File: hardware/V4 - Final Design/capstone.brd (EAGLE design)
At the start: 68.6 x 51.3 mm, 32 parts, among them J1 61300311121, J2 61300311121, J3 61300311121, U1 BMP388, U2 LSM9DS1TR, U3 RFM95W-915S2

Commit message: Schematic Cleanup
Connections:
- net +3V3: now also C3.1; no longer C3.2
- net GND: now also C3.2; no longer C3.1
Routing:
- net +3V3: track 117.5 -> 98.0 mm, vias 3 -> 2
- net GND: track 169.5 -> 154.7 mm
- net N$4: track 6.48 -> 4.67 mm

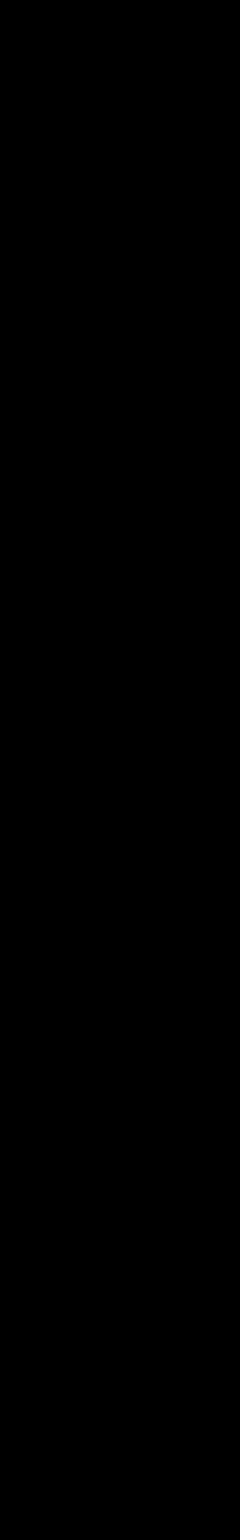
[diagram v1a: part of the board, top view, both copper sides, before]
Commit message: add test points to final design
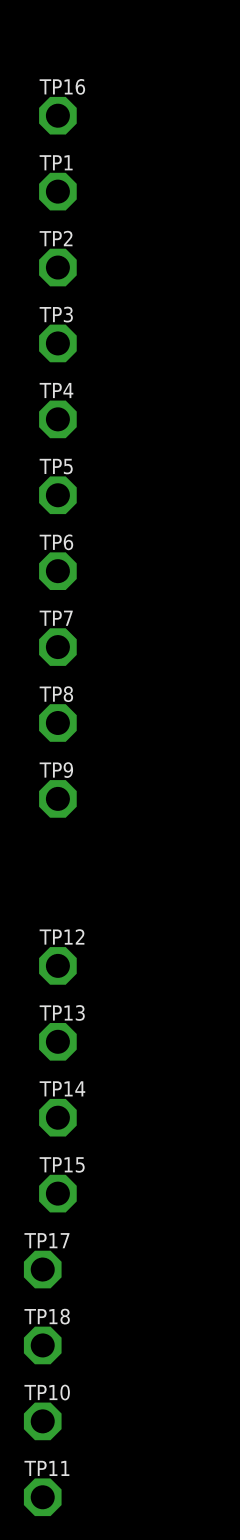
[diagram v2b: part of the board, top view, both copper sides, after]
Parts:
- added TP1, TP10, TP11, TP12, TP13, TP14, TP15, TP16, TP17, TP18, TP2, TP3, TP4, TP5, TP6, TP7, TP8, TP9: PTR1PAD1-20, testpad:P1-20
- R1, R11, R12, R2: value 100 Ohm -> 470 Ohm
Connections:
- net +3V3: now also TP10.TP, TP17.TP, TP4.TP, TP8.TP, TP9.TP
- net GND: now also TP1.TP
- net MISO: now also TP12.TP
- net MOSI: now also TP18.TP
- net RADIO_INT: now also TP15.TP, U$1.15/A1
- net RADIO_RST: now also TP14.TP
- net SCK: now also TP13.TP
- net SCL: now also TP2.TP
- net SDA: now also TP3.TP
- net SERVO1: now also TP5.TP
- net SERVO2: now also TP6.TP
- net SERVO3: now also TP7.TP
- net VBACKUP: now also TP11.TP
- net VIN: now also TP16.TP

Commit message: finalized board design for final design
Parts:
- added H1, H2, H3, H4: MOUNT-HOLE2.8, holes:2,8
- C1, C4: value 10 uF -> 10 u
- C2: value 100 nF -> 100 n
- C3: value 0.1 uF -> 0.1u
- TP1, TP10, TP11, TP12, TP13, TP14, TP15, TP16, TP17, TP18, TP2, TP3, TP4, TP5, TP6, TP7, TP8, TP9: value PTR1PAD1-20 -> PTR1B1,27; device testpad:P1-20 -> testpad:B1,27
- moved TP10 368.1 mm to (63.5, 29.2)
- moved TP17 355.9 mm to (6.35, 39.4)
- moved TP11 354.5 mm to (58.4, 10.2)
- moved TP18 351.5 mm to (23.1, 26.7)
- moved TP13 331.4 mm to (23.4, 31.9)
- moved TP15 328.2 mm to (8.89, 17.8)
- moved TP9 326.6 mm to (39.8, 44.5)
- moved TP14 322.5 mm to (14.0, 17.8)
- moved TP8 318.2 mm to (14.6, 46.5)
- moved TP12 314.7 mm to (23.1, 21.3)
- moved TP3 284.2 mm to (26.7, 41.9)
- moved TP2 277.3 mm to (22.9, 41.9)
- moved TP7 276.7 mm to (19.7, 10.2)
- moved TP6 269.9 mm to (15.9, 10.2)
- moved TP4 264.8 mm to (22.9, 16.5)
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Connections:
- net +3V3: now also TP11.TP; no longer TP10.TP
- net GND: now also TP16.TP; no longer TP1.TP
- net VBACKUP: now also TP10.TP; no longer TP11.TP
- net VIN: now also TP1.TP; no longer TP16.TP
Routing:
- net GPS_TX: track 103.3 -> 21.9 mm
- net GPS_RX: track 101.1 -> 20.0 mm, vias 2 -> 1
- net GND: track 154.7 -> 82.6 mm, vias 11 -> 7
- net RADIO_LED: track 0.00 -> 50.0 mm, vias 0 -> 3
- net ERR_LED: track 0.00 -> 49.8 mm, vias 0 -> 3
- net STATUS_LED: track 0.00 -> 44.5 mm, vias 0 -> 3
- net RADIO_INT: track 0.00 -> 35.6 mm, vias 0 -> 1
- net VIN: track 23.9 -> 56.6 mm
- net RADIO_RST: track 0.00 -> 29.5 mm, vias 0 -> 1
- net VBACKUP: track 0.00 -> 26.9 mm, vias 0 -> 3
- net SERVO1: track 0.00 -> 22.4 mm, vias 0 -> 1
- net +3V3: track 98.0 -> 115.7 mm, vias 2 -> 10
- net SCK: track 35.3 -> 17.7 mm, vias 2 -> 1
- net MISO: track 23.0 -> 39.8 mm, vias 0 -> 2
- net SERVO2: track 0.00 -> 15.9 mm, vias 0 -> 1
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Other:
- board text added: "0.1u"
- board text added: "100n"
- board text added: "10n"
- board text added: "10u"
- board text added: "4.7k"
- board text added: "470"
- board text added: "ANT"
- board text added: "DATA"
- board text added: "ERROR LED"
- board text added: "FIX LED"
- board text added: "POWER LED"
- board text added: "RADIO LED"
- board text added: "STATUS LED"
- board text added: "TP 3.3"
- board text added: "TP BACKUP"
- board text added: "TP GND"
- board text added: "TP GPS PWR"
- board text added: "TP IMU PWR"
- board text added: "TP INT"
- board text added: "TP MISO"
- board text added: "TP MOSI"
- board text added: "TP RADIO PWR"
- board text added: "TP RST"
- board text added: "TP S1"
- board text added: "TP S2"
- board text added: "TP S3"
- board text added: "TP SCK"
- board text added: "TP SCL"
- board text added: "TP SDA"
- board text added: "TP VIN"
- board text added: "VDD"
- board text removed: "SERVO"

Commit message: design update for hardware
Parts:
- removed PWR_LED3: HSMH-C190, LED:LED-0603
- added LED1: HSMH-C190, LED:LED-0603
- R1, R11, R12, R2: value 470 Ohm -> 82 Ohm
- turned LED2 to 0 degrees
- turned LED3 to 0 degrees
- turned LED4 to 0 degrees
- renumbered FIX_LED to LED5, PWR_LED to LED4, PWR_LED1 to LED3, PWR_LED2 to LED2
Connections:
- removed net N$8: LED2.A, R2.1
- new net N$6: LED1.C, R12.1
- net +3V3: now also LED1.A; no longer PWR_LED3.C
- net ERR_LED: now also LED2.A; no longer LED2.C
- net N$10: now also LED3.C, R1.1; no longer LED4.A, R11.1
- net N$7: now also LED2.C, R2.1; no longer PWR_LED3.A, R12.1
- net N$9: now also LED4.C, R11.1; no longer LED3.A, R1.1
- net RADIO_LED: now also LED4.A; no longer LED4.C
- net STATUS_LED: now also LED3.A; no longer LED3.C
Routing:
- net N$6: track 0.00 -> 2.99 mm
- net STATUS_LED: track 44.5 -> 47.1 mm
- net N$8: track 2.22 -> 0.00 mm
- net VIN: track 56.6 -> 54.5 mm
- net N$7: track 3.24 -> 2.22 mm
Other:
- board size 68.6 x 51.3 mm -> 68.6 x 51.8 mm
- board text added: "82"
